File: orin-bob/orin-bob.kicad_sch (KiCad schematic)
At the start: 0 parts

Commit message: Finished schematic for bob
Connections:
- no-connect marks 0 -> 3
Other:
- sheet Connectors ports: added CANH, CANL, CS, SCL, SCLK, SDA, SDI, SDO, UART1_RX1, UART1_TX; removed none
- sheet digital_isolator ports: added 3V3, 3V3_ISO, CAN0_DIN1, CAN0_DOUT1, CANH, CANL, CS, I2C5_CLK1, I2C5_DAT1, SCL, SCLK, SDA, SDI, SDO, SPI1_CS0_N1, SPI1_MISO1, SPI1_MOSI1, SPI1_SCK1, UART1_RX, UART1_RX1, UART1_TX, UART1_TX1; removed none
- sheet orin-connector ports: added 3V3, 5V, CAN0_DIN1, CAN0_DOUT1, I2C5_CLK1, I2C5_DAT1, SPI1_CS0_N1, SPI1_CS1_N1, SPI1_MISO1, SPI1_MOSI1, SPI1_SCK1, UART1_RX1, UART1_TX1; removed none

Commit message: some small changes
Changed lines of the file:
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@@
 			)
 		)
-		(pin "3V3_ISO" output
+		(pin "3V3_ISO" input
 			(at 110.49 36.83 90)
 			(effects

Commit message: Updated bob pcb
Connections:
- no-connect marks 3 -> 1
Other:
- sheet Connectors ports: added GPIOIN_ISO, GPIOOUT_ISO, PWM, UART1_RX; removed UART1_RX1
- sheet digital_isolator ports: added GPIOIN, GPIOIN_ISO, GPIOOUT, GPIOOUT_ISO, PWM, PWM01; removed 3V3, 3V3_ISO
- sheet orin-connector ports: added GPIOOUT, PWM01; removed 3V3, 5V

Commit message: Finished Version 1 BoB pcb
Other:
- sheet orin-connector ports: added GPIOIN; removed none

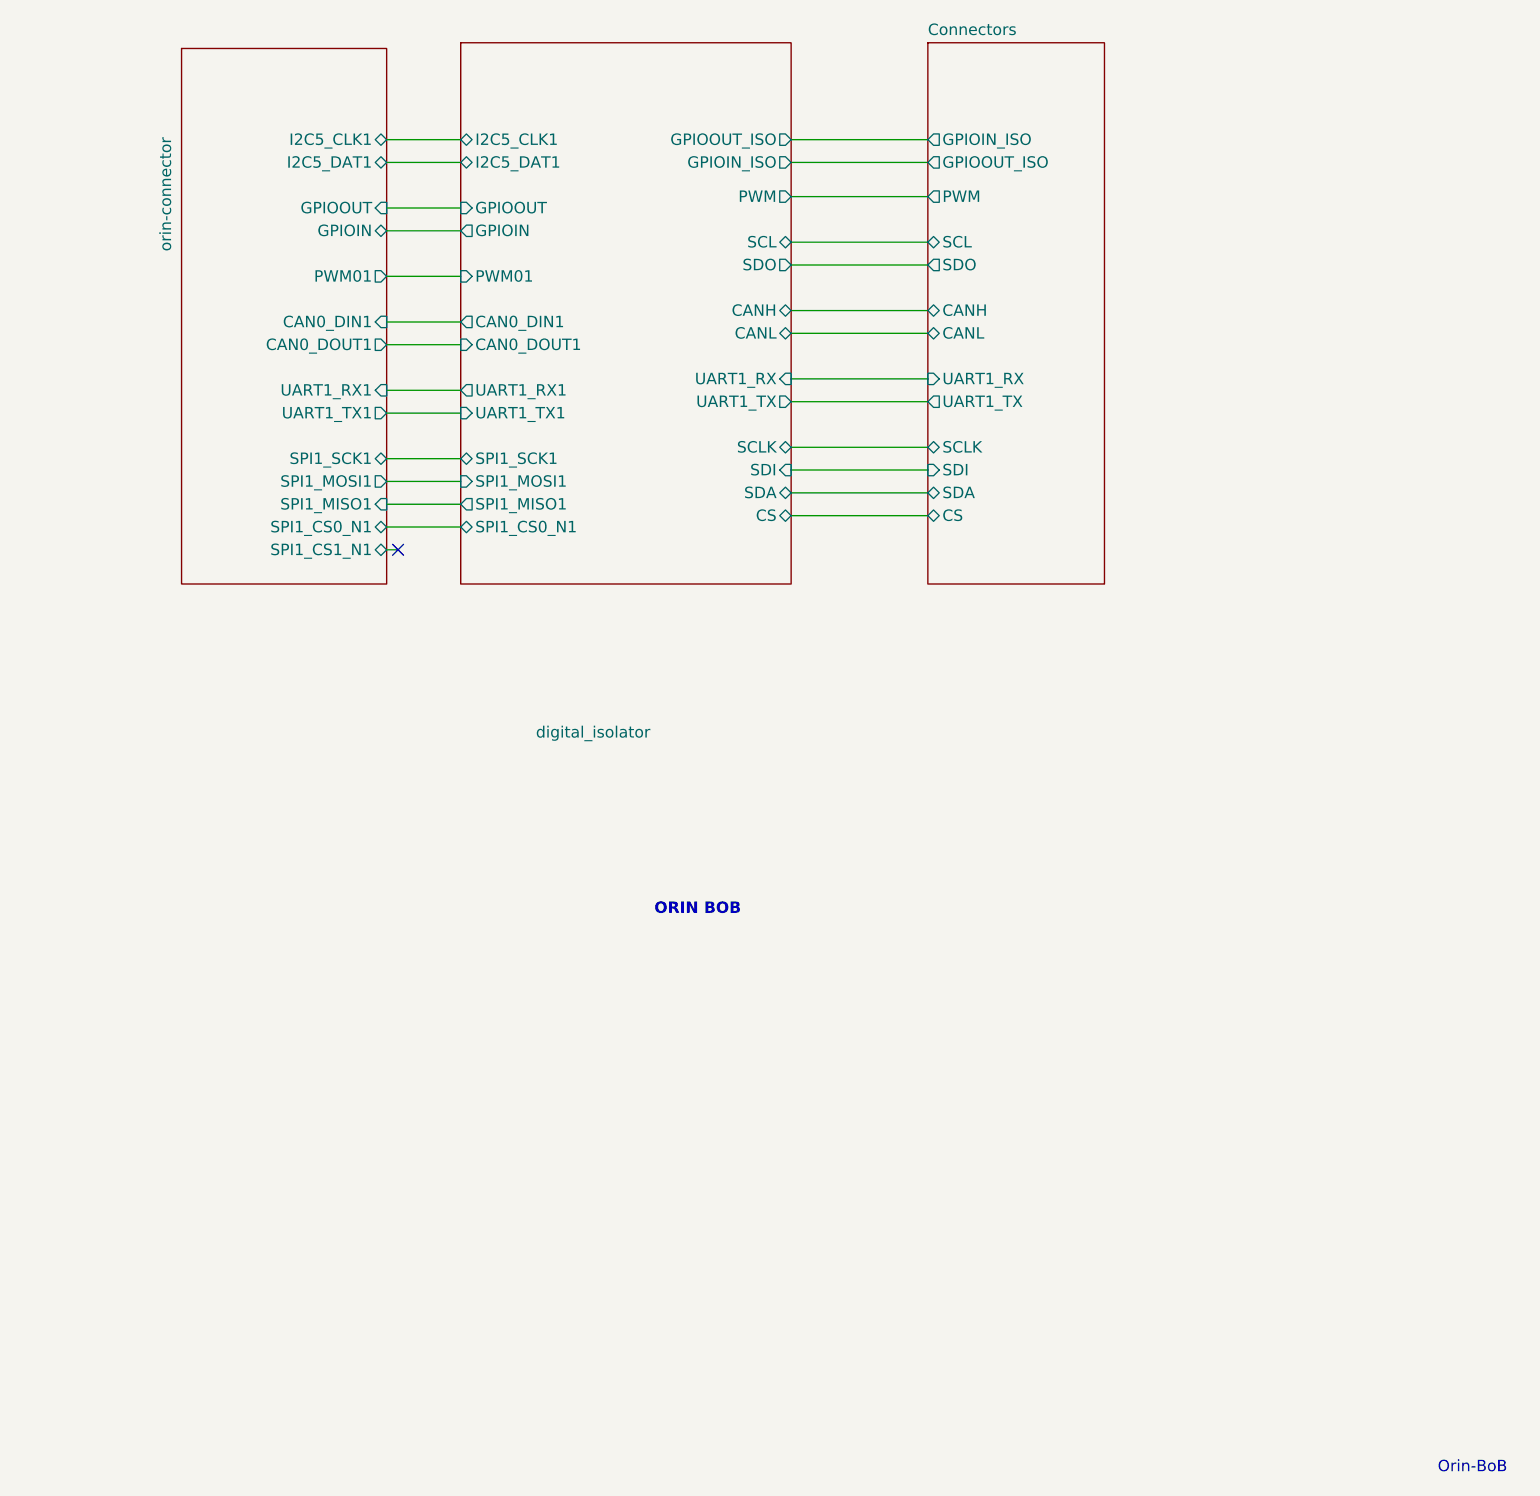
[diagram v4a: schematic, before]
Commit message: Fikset en god del småting i schematic
GPIO IN og OUT var flippet.
Mange små utsene ting.
La til Vortex Logo
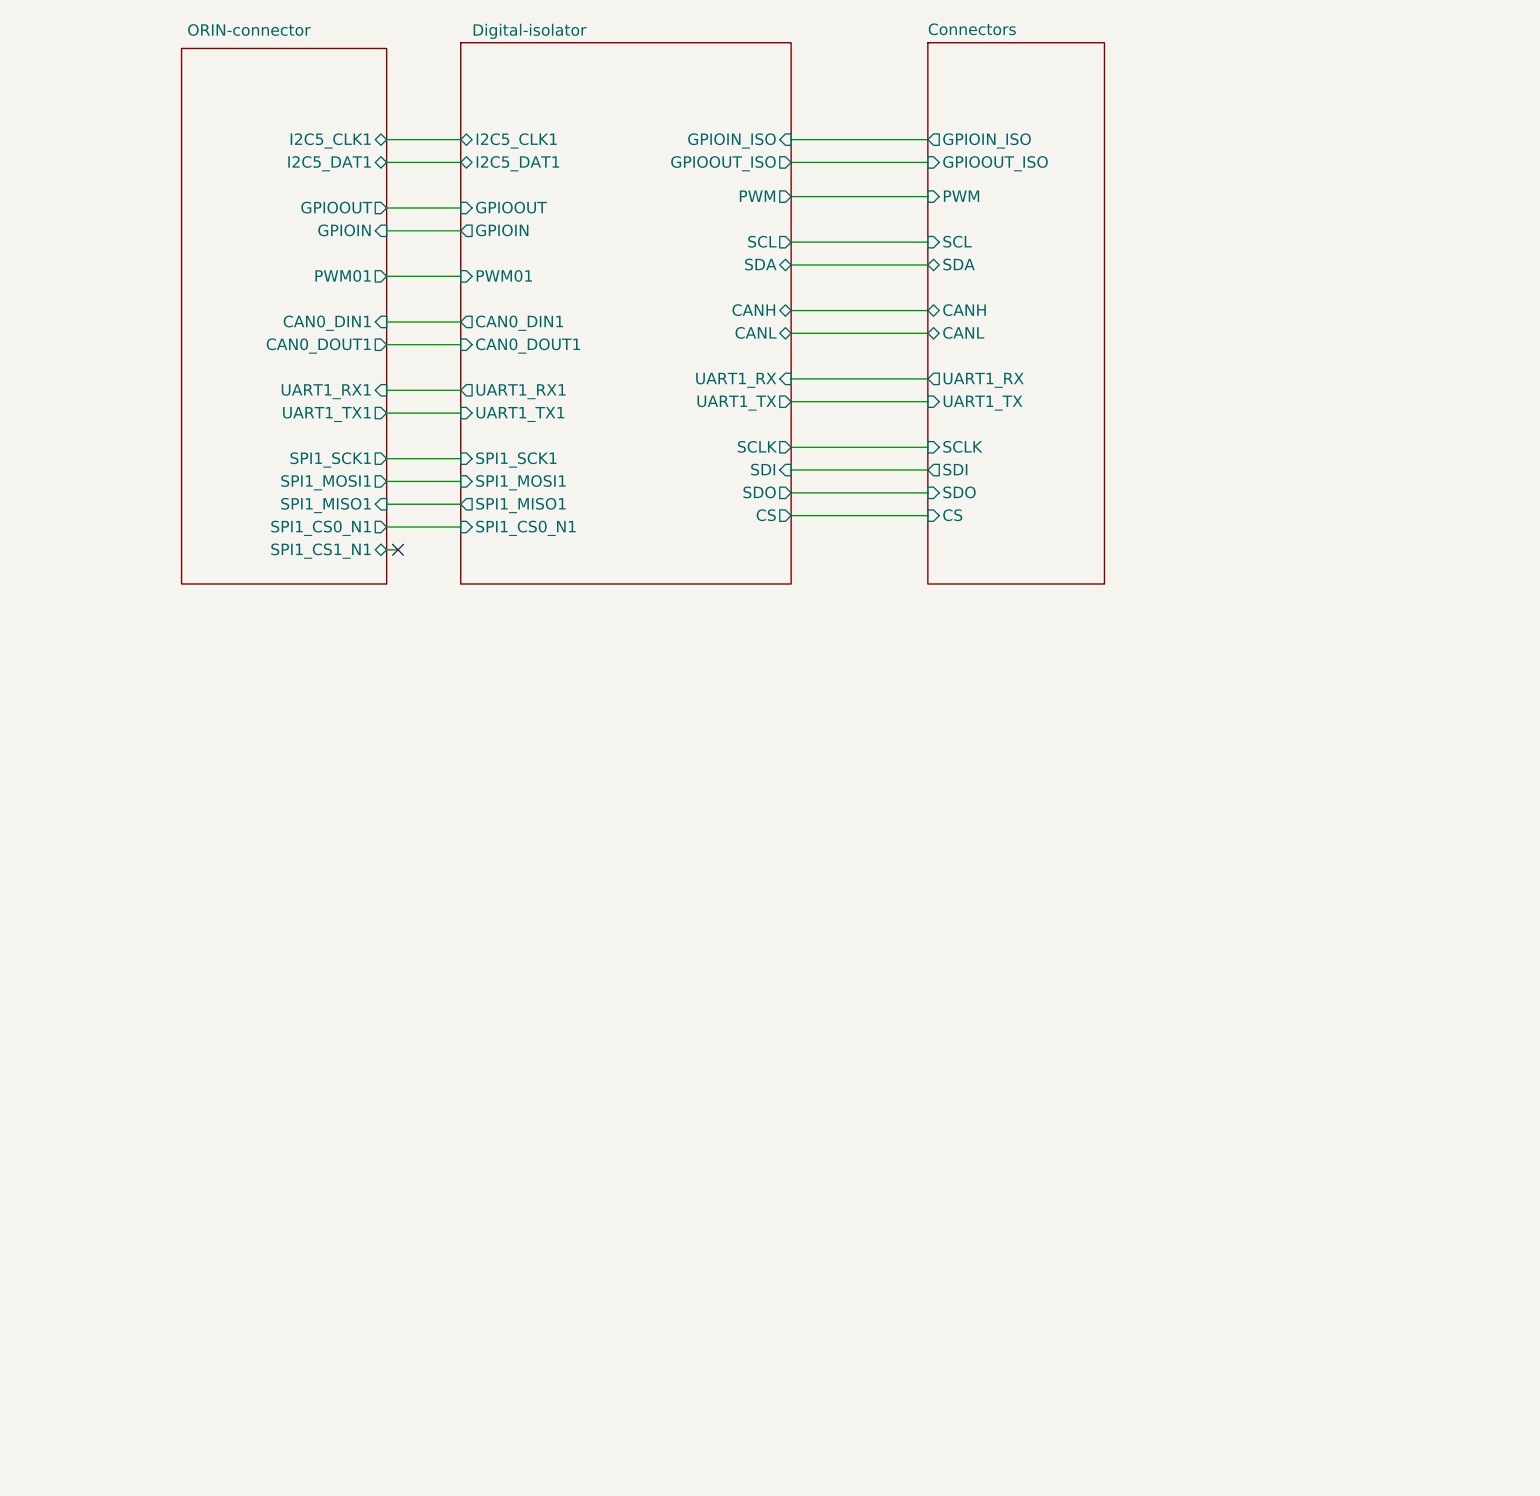
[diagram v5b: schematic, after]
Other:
- sheet digital_isolator renamed Digital-isolator
- sheet orin-connector renamed ORIN-connector
- note removed: "ORIN BOB"
- note removed: "Orin-BoB"
- company: (none) -> Vortex NTNU
- title: (none) -> ORIN-BOB

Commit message: Finished: Orin-BoB
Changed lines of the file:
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@@
 	(wire
 		(pts
-			(xy 71.755 64.77) (xy 80.01 64.77)
-		)
-		(stroke
-			(width 0)
-			(type default)
-		)
-	)
-	(wire
-		(pts
-			(xy 71.755 69.85) (xy 80.01 69.85)
+			(xy 68.58 64.77) (xy 80.01 64.77)
+		)
+		(stroke
+			(width 0)
+			(type default)
+		)
+	)
+	(wire
+		(pts
+			(xy 68.58 69.85) (xy 80.01 69.85)
 		)
 		(stroke
@@
 	(wire
 		(pts
-			(xy 71.755 85.09) (xy 80.01 85.09)
+			(xy 68.58 85.09) (xy 80.01 85.09)
 		)
 		(stroke
@@
 	(wire
 		(pts
-			(xy 71.755 77.47) (xy 80.01 77.47)
+			(xy 68.58 77.47) (xy 80.01 77.47)
 		)
 		(stroke
@@
 	(wire
 		(pts
-			(xy 71.755 82.55) (xy 80.01 82.55)
-		)
-		(stroke
-			(width 0)
-			(type default)
-		)
-	)
-	(wire
-		(pts
-			(xy 71.755 87.63) (xy 73.025 87.63)
-		)
-		(stroke
-			(width 0)
-			(type default)
-		)
-	)
-	(wire
-		(pts
-			(xy 71.755 52.07) (xy 80.01 52.07)
+			(xy 68.58 82.55) (xy 80.01 82.55)
+		)
+		(stroke
+			(width 0)
+			(type default)
+		)
+	)
+	(wire
+		(pts
+			(xy 68.58 87.63) (xy 73.025 87.63)
+		)
+		(stroke
+			(width 0)
+			(type default)
+		)
+	)
+	(wire
+		(pts
+			(xy 68.58 52.07) (xy 80.01 52.07)
 		)
 		(stroke
@@
 	(wire
 		(pts
-			(xy 71.755 80.01) (xy 80.01 80.01)
-		)
-		(stroke
-			(width 0)
-			(type default)
-		)
-	)
-	(wire
-		(pts
-			(xy 71.755 41.91) (xy 80.01 41.91)
+			(xy 68.58 80.01) (xy 80.01 80.01)
+		)
+		(stroke
+			(width 0)
+			(type default)
+		)
+	)
+	(wire
+		(pts
+			(xy 68.58 41.91) (xy 80.01 41.91)
 		)
 		(stroke
@@
 	(wire
 		(pts
-			(xy 71.755 49.53) (xy 80.01 49.53)
+			(xy 68.58 49.53) (xy 80.01 49.53)
 		)
 		(stroke
@@
 	(wire
 		(pts
-			(xy 71.755 57.15) (xy 80.01 57.15)
+			(xy 68.58 57.15) (xy 80.01 57.15)
 		)
 		(stroke
@@
 	(wire
 		(pts
-			(xy 71.755 62.23) (xy 80.01 62.23)
-		)
-		(stroke
-			(width 0)
-			(type default)
-		)
-	)
-	(wire
-		(pts
-			(xy 71.755 72.39) (xy 80.01 72.39)
-		)
-		(stroke
-			(width 0)
-			(type default)
-		)
-	)
-	(wire
-		(pts
-			(xy 71.755 44.45) (xy 80.01 44.45)
+			(xy 68.58 62.23) (xy 80.01 62.23)
+		)
+		(stroke
+			(width 0)
+			(type default)
+		)
+	)
+	(wire
+		(pts
+			(xy 68.58 72.39) (xy 80.01 72.39)
+		)
+		(stroke
+			(width 0)
+			(type default)
+		)
+	)
+	(wire
+		(pts
+			(xy 68.58 44.45) (xy 80.01 44.45)
 		)
 		(stroke
@@
 	)
 	(sheet
-		(at 48.895 31.75)
+		(at 45.72 31.75)
 		(size 22.86 59.69)
 		(exclude_from_sim no)
@@
 		)
 		(property "Sheetname" "ORIN-connector"
-			(at 49.53 30.48 0)
+			(at 46.355 30.48 0)
 			(show_name no)
 			(do_not_autoplace no)
@@
 		)
 		(property "Sheetfile" "orin-connector.kicad_sch"
-			(at 48.895 66.3706 0)
+			(at 45.72 66.3706 0)
 			(hide yes)
 			(show_name no)
@@
 		)
 		(pin "CAN0_DIN1" input
-			(at 71.755 62.23 0)
+			(at 68.58 62.23 0)
 			(effects
 				(font
@@
 		)
 		(pin "CAN0_DOUT1" output
-			(at 71.755 64.77 0)
+			(at 68.58 64.77 0)
 			(effects
 				(font
@@
 		)
 		(pin "I2C5_CLK1" bidirectional
-			(at 71.755 41.91 0)
+			(at 68.58 41.91 0)
 			(effects
 				(font
@@
 		)
 		(pin "I2C5_DAT1" bidirectional
-			(at 71.755 44.45 0)
+			(at 68.58 44.45 0)
 			(effects
 				(font
@@
 		)
 		(pin "SPI1_CS0_N1" output
-			(at 71.755 85.09 0)
+			(at 68.58 85.09 0)
 			(effects
 				(font
@@
 		)
 		(pin "SPI1_CS1_N1" bidirectional
-			(at 71.755 87.63 0)
+			(at 68.58 87.63 0)
 			(effects
 				(font
@@
 		)
 		(pin "SPI1_MISO1" input
-			(at 71.755 82.55 0)
+			(at 68.58 82.55 0)
 			(effects
 				(font
@@
 		)
 		(pin "SPI1_MOSI1" output
-			(at 71.755 80.01 0)
+			(at 68.58 80.01 0)
 			(effects
 				(font
@@
 		)
 		(pin "SPI1_SCK1" output
-			(at 71.755 77.47 0)
+			(at 68.58 77.47 0)
 			(effects
 				(font
@@
 		)
 		(pin "UART1_RX1" input
-			(at 71.755 69.85 0)
+			(at 68.58 69.85 0)
 			(effects
 				(font
@@
 		)
 		(pin "UART1_TX1" output
-			(at 71.755 72.39 0)
+			(at 68.58 72.39 0)
 			(effects
 				(font
@@
 		)
 		(pin "GPIOOUT" output
-			(at 71.755 49.53 0)
+			(at 68.58 49.53 0)
 			(effects
 				(font
@@
 		)
 		(pin "PWM01" output
-			(at 71.755 57.15 0)
+			(at 68.58 57.15 0)
 			(effects
 				(font
@@
 		)
 		(pin "GPIOIN" input
-			(at 71.755 52.07 0)
-			(effects
-				(font
+			(at 68.58 52.07 0)
+			(effects
+				(font
